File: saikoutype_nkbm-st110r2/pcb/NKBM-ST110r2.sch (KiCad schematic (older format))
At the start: 260 parts, among them K001 CHRY_MX, K021 CHRY_MX, K031 CHRY_MX, K041 CHRY_MX, K051 CHRY_MX, K061 CHRY_MX, K071 CHRY_MX, K081 CHRY_MX, K091 CHRY_MX, K0B1 CHRY_MX, K0C1 CHRY_MX, K0D1 CHRY_MX, K0E1 CHRY_MX, K101 CHRY_MX, K111 CHRY_MX, K121 CHRY_MX, K131 CHRY_MX, K141 CHRY_MX, K151 CHRY_MX, K161 CHRY_MX, K171 CHRY_MX, K181 CHRY_MX, K191 CHRY_MX, K1A1 CHRY_MX, K1B1 CHRY_MX, K1C1 CHRY_MX, K1D1 CHRY_MX, K1E1 CHRY_MX, K1E2 CHRY_MX, K201 CHRY_MX, K211 CHRY_MX, K221 CHRY_MX, K231 CHRY_MX, K241 CHRY_MX, K251 CHRY_MX, K261 CHRY_MX, K271 CHRY_MX, K281 CHRY_MX, K291 CHRY_MX, K2A1 CHRY_MX, K2B1 CHRY_MX, K2C1 CHRY_MX, K301 CHRY_MX, K311 CHRY_MX, K321 CHRY_MX, K331 CHRY_MX, K341 CHRY_MX, K351 CHRY_MX, K361 CHRY_MX, K371 CHRY_MX, K381 CHRY_MX, K391 CHRY_MX, K3A1 CHRY_MX, K3B1 CHRY_MX, K3C1 CHRY_MX, K3C2 CHRY_MX, K3E1 CHRY_MX, K3E2 CHRY_MX, K401 CHRY_MX, K402 CHRY_MX, K411 CHRY_MX, K421 CHRY_MX, K431 CHRY_MX, K441 CHRY_MX, K451 CHRY_MX, K461 CHRY_MX, K471 CHRY_MX, K481 CHRY_MX, K491 CHRY_MX, K4A1 CHRY_MX, K4B1 CHRY_MX, K4C1 CHRY_MX, K4D1 CHRY_MX, K4D2 CHRY_MX, K501 CHRY_MX, K511 CHRY_MX, K512 CHRY_MX, K521 CHRY_MX, K522 CHRY_MX, K531 CHRY_MX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

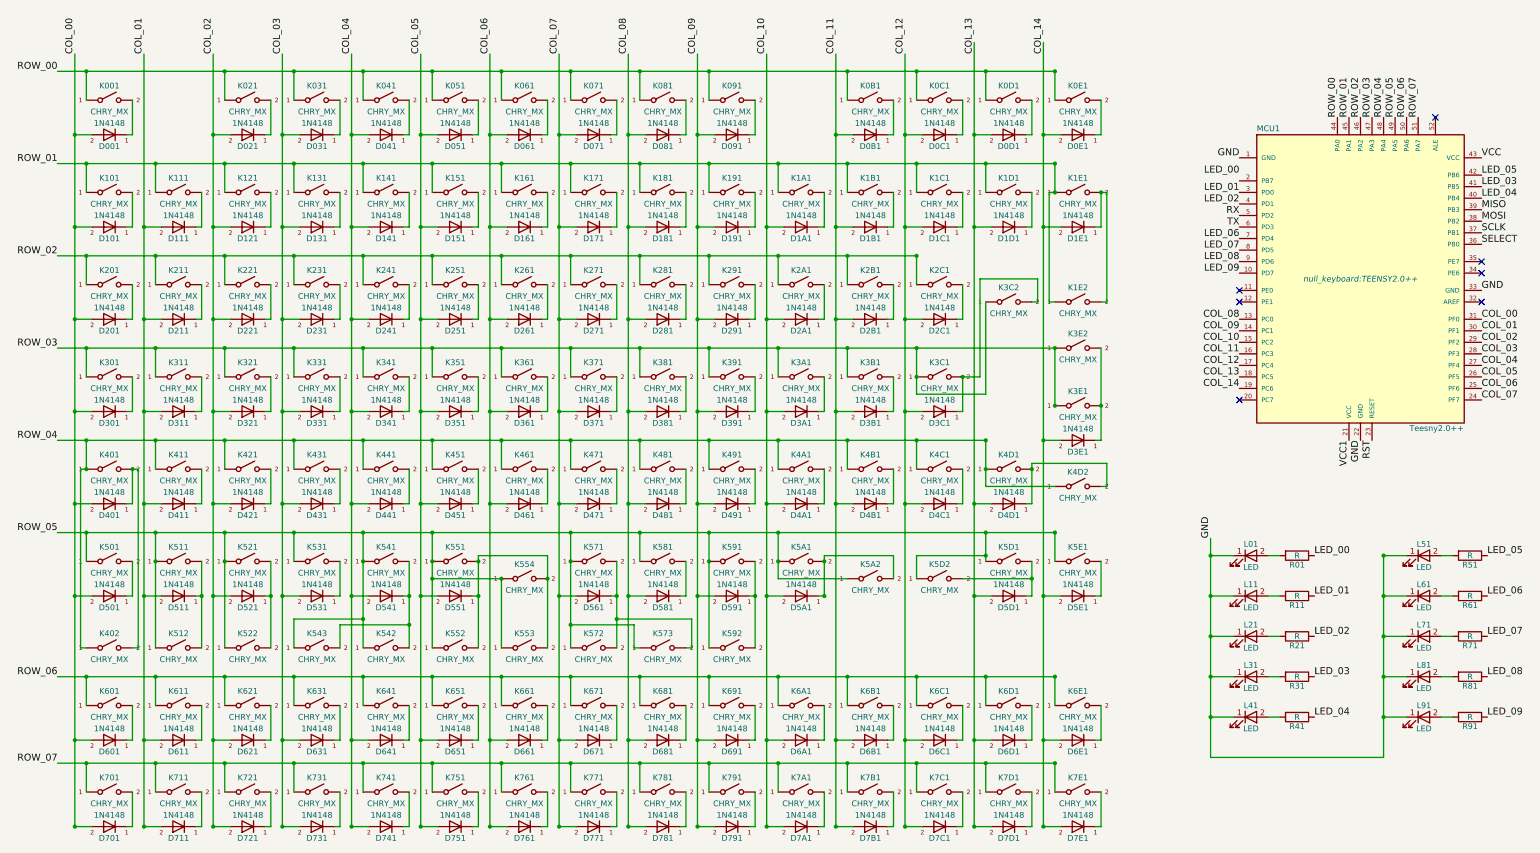
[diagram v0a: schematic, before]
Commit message: Updated Schematic to be more readable.
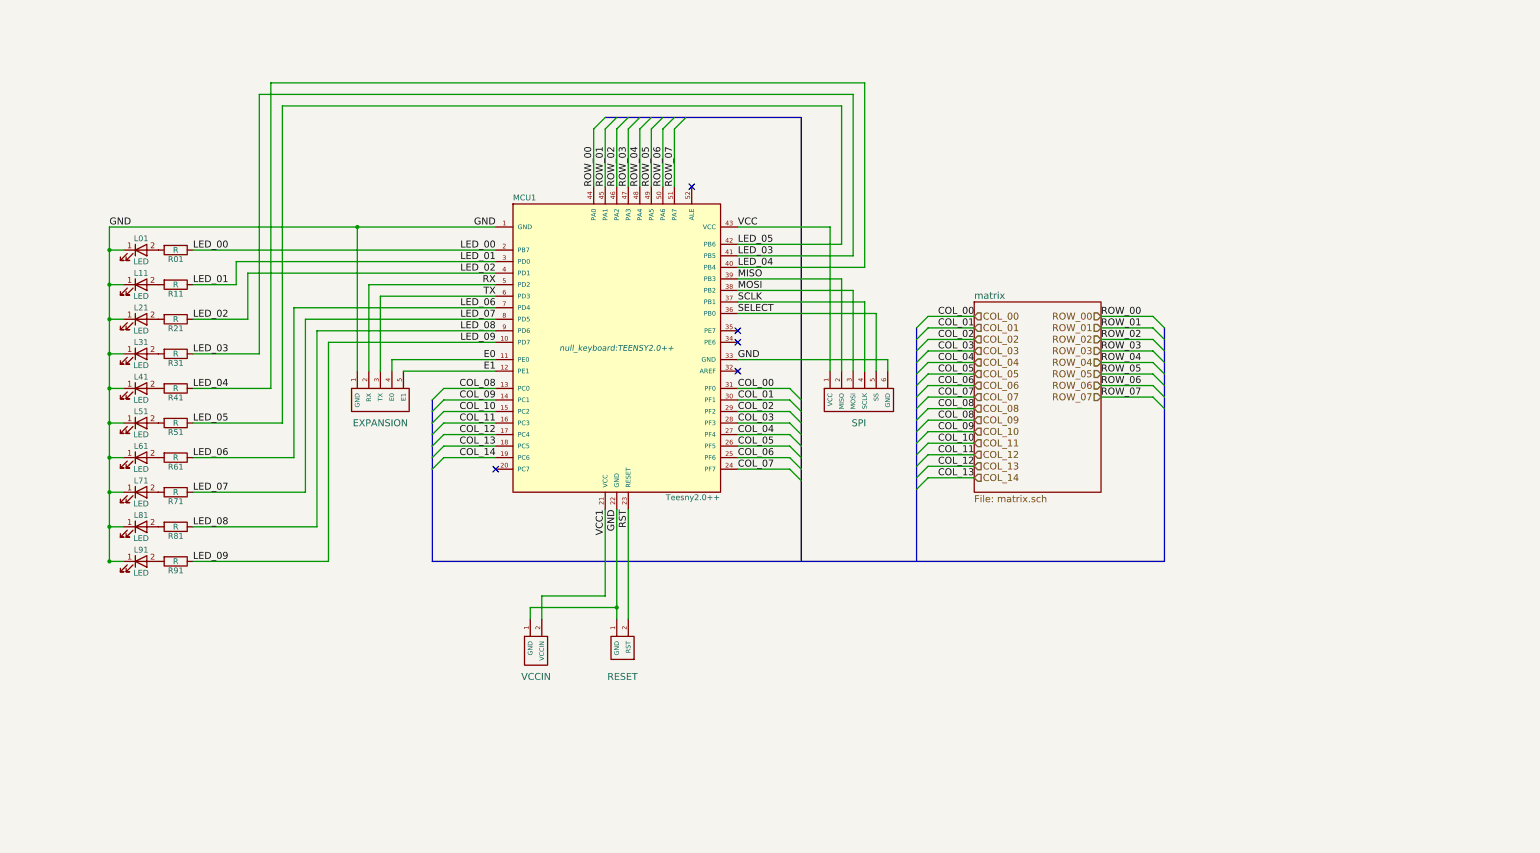
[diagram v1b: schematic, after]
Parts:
- removed D001, D021, D031, D041, D051, D061, D071, D081, D091, D0B1, D0C1, D0D1, D0E1, D101, D111, D121, D131, D141, D151, D161, D171, D181, D191, D1A1, D1B1, D1C1, D1D1, D1E1, D201, D211, D221, D231, D241, D251, D261, D271, D281, D291, D2A1, D2B1, D2C1, D301, D311, D321, D331, D341, D351, D361, D371, D381, D391, D3A1, D3B1, D3C1, D3E1, D401, D411, D421, D431, D441, D451, D461, D471, D481, D491, D4A1, D4B1, D4C1, D4D1, D501, D511, D521, D531, D541, D551, D561, D581, D591, D5A1, D5D1, D5E1, D601, D611, D621, D631, D641, D651, D661, D671, D681, D691, D6A1, D6B1, D6C1, D6D1, D6E1, D701, D711, D721, D731, D741, D751, D761, D771, D781, D791, D7A1, D7B1, D7C1, D7D1, D7E1: 1N4148, null_keyboard:DIODE, symbol 1N4148
- removed K001, K021, K031, K041, K051, K061, K071, K081, K091, K0B1, K0C1, K0D1, K0E1, K101, K111, K121, K131, K141, K151, K161, K171, K181, K191, K1A1, K1B1, K1C1, K1D1, K1E2, K211, K221, K231, K241, K251, K261, K271, K281, K291, K2A1, K2B1, K2C1, K311, K321, K331, K341, K351, K361, K371, K381, K391, K3A1, K3B1, K411, K421, K431, K441, K461, K471, K481, K491, K4A1, K4B1, K4C1, K511, K531, K5D1, K601, K611, K621, K631, K641, K651, K661, K671, K681, K691, K6A1, K6B1, K6C1, K6D1, K6E1, K701, K711, K721, K731, K741, K751, K761, K771, K781, K791, K7A1, K7B1, K7C1, K7D1, K7E1: CHRY_MX, null_keyboard:CHERRY_PLATE_100H, symbol SW_SPST-RESCUE-null-ukb-full
- removed K1E1, K3E1, K541, K571: CHRY_MX, null_keyboard:CHERRY_PLATE_200H, symbol SW_SPST-RESCUE-null-ukb-full
- removed K201, K3C1, K3C2: CHRY_MX, null_keyboard:CHERRY_PLATE_150H, symbol SW_SPST-RESCUE-null-ukb-full
- removed K301, K4D1: CHRY_MX, null_keyboard:CHERRY_PLATE_175H, symbol SW_SPST-RESCUE-null-ukb-full
- removed K3E2, K401, K542, K573: CHRY_MX, null_keyboard:CHERRY_PLATE_225H, symbol SW_SPST-RESCUE-null-ukb-full
- removed K402, K451, K501, K512, K521, K522, K543, K553, K554, K572, K581, K591, K592, K5A1, K5A2, K5D2, K5E1: CHRY_MX, null_keyboard:CHERRY_PLATE_125H, symbol SW_SPST-RESCUE-null-ukb-full
- removed K4D2: CHRY_MX, null_keyboard:CHERRY_PLATE_275H, symbol SW_SPST-RESCUE-null-ukb-full
- removed K551: CHRY_MX, null_keyboard:CHERRY_PLATE_625H, symbol SW_SPST-RESCUE-null-ukb-full
- removed K552: CHRY_MX, null_keyboard:CHERRY_PLATE_450H, symbol SW_SPST-RESCUE-null-ukb-full
- added H11: SPI, symbol SPI_HEADER
- added H21: EXPANSION, symbol SERIAL_HEADER
- added H31: RESET, symbol RST_HEADER
- added H41: VCCIN, symbol VCCIN_HEADER
- L01, L41, L51, L61, L71, L81, L91: footprint null_keyboard:LED_3MM -> (none)
- L11, L31: footprint null_keyboard:LED_3MM1 -> (none)
- L21: footprint null_keyboard:LED_3MM2 -> (none)
- R01, R11, R21, R31, R41, R51, R61, R71, R81, R91: footprint null_keyboard:RESISTOR -> (none)
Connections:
- net COL_09 is gone; now on net COL_08: MCU1.14 (PC1)
- net COL_10 is gone; now on net COL_08: MCU1.15 (PC2)
- net COL_11 is gone; now on net COL_08: MCU1.16 (PC3)
- net COL_12 is gone; now on net COL_08: MCU1.17 (PC4)
- net COL_13 is gone; now on net COL_08: MCU1.18 (PC5)
- net COL_14 is gone; now on net COL_08: MCU1.19 (PC6)
- net GND: now also H11.6 (GND), H21.1 (GND), H31.1 (GND), H41.1 (GND)
- net LED_00: now also MCU1.2 (PB7)
- net MISO: now also H11.2 (MISO)
- net MOSI: now also H11.3 (MOSI)
- net RST: now also H31.2 (RST)
- net RX: now also H21.2 (RX)
- net SCLK: now also H11.4 (SCLK)
- net SELECT: now also H11.5 (SS)
- net TX: now also H21.3 (TX)
- net VCC: now also H11.1 (VCC)
- net VCC1: now also H41.2 (VCCIN)
- net E0: now reaches MCU1.11 (PE0)
- net E0: now also H21.4 (E0)
- net E1: now reaches MCU1.12 (PE1)
- net E1: now also H21.5 (E1)
- no-connect marks 7 -> 5
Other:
- moved on the sheet: MCU1

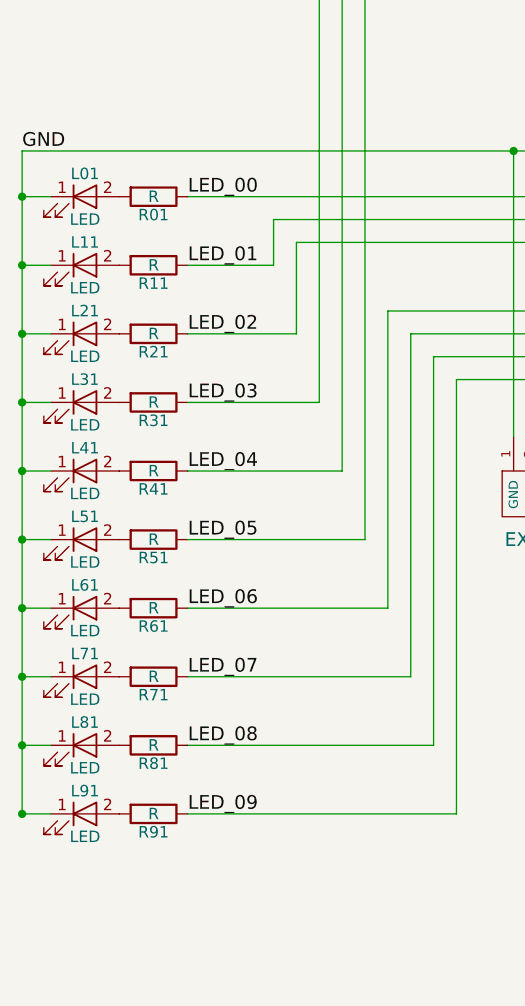
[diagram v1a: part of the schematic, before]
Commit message: Complete reannotation of schematic and PCB.
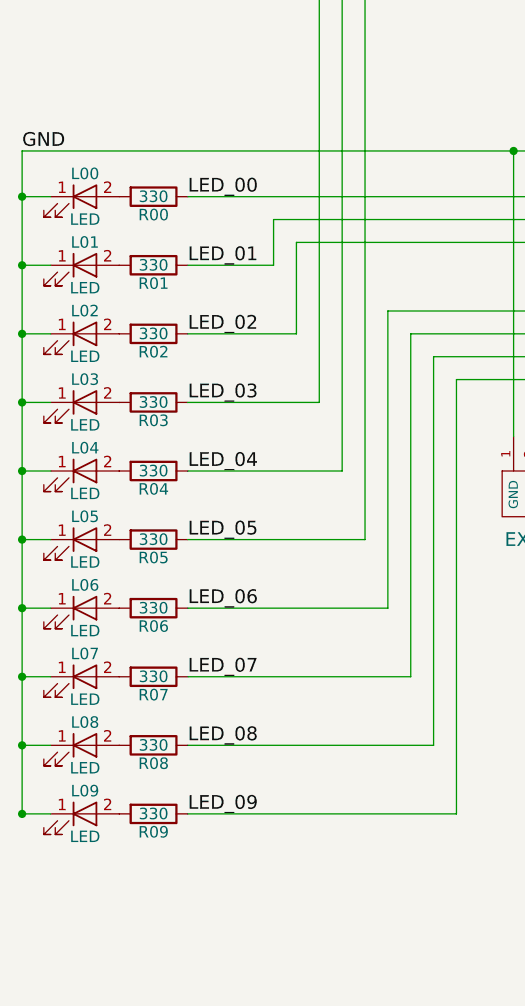
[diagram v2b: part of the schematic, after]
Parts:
- R00: renamed from R01; value R -> 330
- R01: renamed from R11; value R -> 330
- R02: renamed from R21; value R -> 330
- R03: renamed from R31; value R -> 330
- R04: renamed from R41; value R -> 330
- R05: renamed from R51; value R -> 330
- R06: renamed from R61; value R -> 330
- R07: renamed from R71; value R -> 330
- R08: renamed from R81; value R -> 330
- R09: renamed from R91; value R -> 330
- renumbered L01 to L00, L11 to L01, L21 to L02, L31 to L03, L41 to L04, L51 to L05, L61 to L06, L71 to L07, L81 to L08, L91 to L09
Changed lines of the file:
@@
 LED_05
 $Comp
-L R R01
+L R R00
 U 1 1 5A70D797
 P 1925 2600
-F 0 "R01" V 2005 2600 50  0000 C CNN
-F 1 "R" V 1925 2600 50  0000 C CNN
+F 0 "R00" V 2005 2600 50  0000 C CNN
+F 1 "330" V 1925 2600 50  0000 C CNN
 F 2 "" V 1855 2600 50  0000 C CNN
 F 3 "" H 1925 2600 50  0000 C CNN
@@
 $EndComp
 $Comp
-L LED L01
+L LED L00
 U 1 1 5A70D980
 P 1625 2600
-F 0 "L01" H 1625 2700 50  0000 C CNN
+F 0 "L00" H 1625 2700 50  0000 C CNN
 F 1 "LED" H 1625 2500 50  0000 C CNN
 F 2 "" H 1625 2600 50  0000 C CNN
@@
 $EndComp
 $Comp
-L R R11
+L R R01
 U 1 1 5A70DCBF
 P 1925 2900
-F 0 "R11" V 2005 2900 50  0000 C CNN
-F 1 "R" V 1925 2900 50  0000 C CNN
+F 0 "R01" V 2005 2900 50  0000 C CNN
+F 1 "330" V 1925 2900 50  0000 C CNN
 F 2 "" V 1855 2900 50  0000 C CNN
 F 3 "" H 1925 2900 50  0000 C CNN
@@
 $EndComp
 $Comp
-L LED L11
+L LED L01
 U 1 1 5A70DCC6
 P 1625 2900
-F 0 "L11" H 1625 3000 50  0000 C CNN
+F 0 "L01" H 1625 3000 50  0000 C CNN
 F 1 "LED" H 1625 2800 50  0000 C CNN
 F 2 "" H 1625 2900 50  0000 C CNN
@@
 $EndComp
 $Comp
-L R R21
+L R R02
 U 1 1 5A70DF15
 P 1925 3200
-F 0 "R21" V 2005 3200 50  0000 C CNN
-F 1 "R" V 1925 3200 50  0000 C CNN
+F 0 "R02" V 2005 3200 50  0000 C CNN
+F 1 "330" V 1925 3200 50  0000 C CNN
 F 2 "" V 1855 3200 50  0000 C CNN
 F 3 "" H 1925 3200 50  0000 C CNN
@@
 $EndComp
 $Comp
-L LED L21
+L LED L02
 U 1 1 5A70DF1C
 P 1625 3200
-F 0 "L21" H 1625 3300 50  0000 C CNN
+F 0 "L02" H 1625 3300 50  0000 C CNN
 F 1 "LED" H 1625 3100 50  0000 C CNN
 F 2 "" H 1625 3200 50  0000 C CNN
@@
 $EndComp
 $Comp
-L R R31
+L R R03
 U 1 1 5A70DF23
 P 1925 3500
-F 0 "R31" V 2005 3500 50  0000 C CNN
-F 1 "R" V 1925 3500 50  0000 C CNN
+F 0 "R03" V 2005 3500 50  0000 C CNN
+F 1 "330" V 1925 3500 50  0000 C CNN
 F 2 "" V 1855 3500 50  0000 C CNN
 F 3 "" H 1925 3500 50  0000 C CNN
@@
 $EndComp
 $Comp
-L LED L31
+L LED L03
 U 1 1 5A70DF2A
 P 1625 3500
-F 0 "L31" H 1625 3600 50  0000 C CNN
+F 0 "L03" H 1625 3600 50  0000 C CNN
 F 1 "LED" H 1625 3400 50  0000 C CNN
 F 2 "" H 1625 3500 50  0000 C CNN
@@
 $EndComp
 $Comp
-L R R41
+L R R04
 U 1 1 5A70E33E
 P 1925 3800
-F 0 "R41" V 2005 3800 50  0000 C CNN
-F 1 "R" V 1925 3800 50  0000 C CNN
+F 0 "R04" V 2005 3800 50  0000 C CNN
+F 1 "330" V 1925 3800 50  0000 C CNN
 F 2 "" V 1855 3800 50  0000 C CNN
 F 3 "" H 1925 3800 50  0000 C CNN
@@
 $EndComp
 $Comp
-L LED L41
+L LED L04
 U 1 1 5A70E345
 P 1625 3800
-F 0 "L41" H 1625 3900 50  0000 C CNN
+F 0 "L04" H 1625 3900 50  0000 C CNN
 F 1 "LED" H 1625 3700 50  0000 C CNN
 F 2 "" H 1625 3800 50  0000 C CNN
@@
 $EndComp
 $Comp
-L R R51
+L R R05
 U 1 1 5A70E34C
 P 1925 4100
-F 0 "R51" V 2005 4100 50  0000 C CNN
-F 1 "R" V 1925 4100 50  0000 C CNN
+F 0 "R05" V 2005 4100 50  0000 C CNN
+F 1 "330" V 1925 4100 50  0000 C CNN
 F 2 "" V 1855 4100 50  0000 C CNN
 F 3 "" H 1925 4100 50  0000 C CNN
@@
 $EndComp
 $Comp
-L LED L51
+L LED L05
 U 1 1 5A70E353
 P 1625 4100
-F 0 "L51" H 1625 4200 50  0000 C CNN
+F 0 "L05" H 1625 4200 50  0000 C CNN
 F 1 "LED" H 1625 4000 50  0000 C CNN
 F 2 "" H 1625 4100 50  0000 C CNN
@@
 $EndComp
 $Comp
-L R R61
+L R R06
 U 1 1 5A70E35A
 P 1925 4400
-F 0 "R61" V 2005 4400 50  0000 C CNN
-F 1 "R" V 1925 4400 50  0000 C CNN
+F 0 "R06" V 2005 4400 50  0000 C CNN
+F 1 "330" V 1925 4400 50  0000 C CNN
 F 2 "" V 1855 4400 50  0000 C CNN
 F 3 "" H 1925 4400 50  0000 C CNN
@@
 $EndComp
 $Comp
-L LED L61
+L LED L06
 U 1 1 5A70E361
 P 1625 4400
-F 0 "L61" H 1625 4500 50  0000 C CNN
+F 0 "L06" H 1625 4500 50  0000 C CNN
 F 1 "LED" H 1625 4300 50  0000 C CNN
 F 2 "" H 1625 4400 50  0000 C CNN
@@
 $EndComp
 $Comp
-L R R71
+L R R07
 U 1 1 5A70E368
 P 1925 4700
-F 0 "R71" V 2005 4700 50  0000 C CNN
-F 1 "R" V 1925 4700 50  0000 C CNN
+F 0 "R07" V 2005 4700 50  0000 C CNN
+F 1 "330" V 1925 4700 50  0000 C CNN
 F 2 "" V 1855 4700 50  0000 C CNN
 F 3 "" H 1925 4700 50  0000 C CNN
@@
 $EndComp
 $Comp
-L LED L71
+L LED L07
 U 1 1 5A70E36F
 P 1625 4700
-F 0 "L71" H 1625 4800 50  0000 C CNN
+F 0 "L07" H 1625 4800 50  0000 C CNN
 F 1 "LED" H 1625 4600 50  0000 C CNN
 F 2 "" H 1625 4700 50  0000 C CNN
@@
 $EndComp
 $Comp
-L R R81
+L R R08
 U 1 1 5A70E8C2
 P 1925 5000
-F 0 "R81" V 2005 5000 50  0000 C CNN
-F 1 "R" V 1925 5000 50  0000 C CNN
+F 0 "R08" V 2005 5000 50  0000 C CNN
+F 1 "330" V 1925 5000 50  0000 C CNN
 F 2 "" V 1855 5000 50  0000 C CNN
 F 3 "" H 1925 5000 50  0000 C CNN
@@
 $EndComp
 $Comp
-L LED L81
+L LED L08
 U 1 1 5A70E8C9
 P 1625 5000
-F 0 "L81" H 1625 5100 50  0000 C CNN
+F 0 "L08" H 1625 5100 50  0000 C CNN
 F 1 "LED" H 1625 4900 50  0000 C CNN
 F 2 "" H 1625 5000 50  0000 C CNN
@@
 $EndComp
 $Comp
-L R R91
+L R R09
 U 1 1 5A70E8D0
 P 1925 5300
-F 0 "R91" V 2005 5300 50  0000 C CNN
-F 1 "R" V 1925 5300 50  0000 C CNN
+F 0 "R09" V 2005 5300 50  0000 C CNN
+F 1 "330" V 1925 5300 50  0000 C CNN
 F 2 "" V 1855 5300 50  0000 C CNN
 F 3 "" H 1925 5300 50  0000 C CNN
@@
 $EndComp
 $Comp
-L LED L91
+L LED L09
 U 1 1 5A70E8D7
 P 1625 5300
-F 0 "L91" H 1625 5400 50  0000 C CNN
+F 0 "L09" H 1625 5400 50  0000 C CNN
 F 1 "LED" H 1625 5200 50  0000 C CNN
 F 2 "" H 1625 5300 50  0000 C CNN
